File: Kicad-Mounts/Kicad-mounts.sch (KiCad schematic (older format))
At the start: 10 parts, among them P1 CONN_10, P2 CONN_10, P3 CONN_6X2, P6 CONN_3, U2 TPS77033

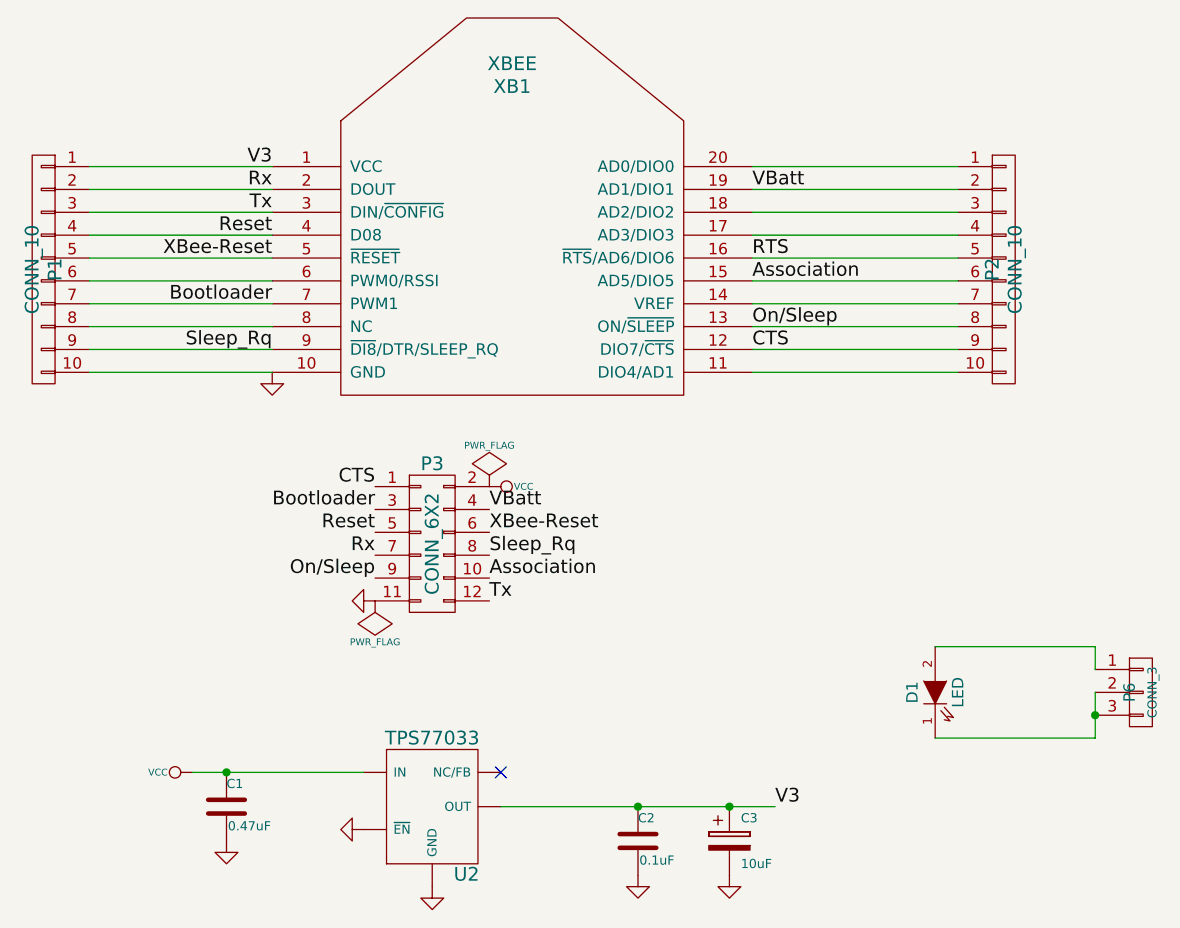
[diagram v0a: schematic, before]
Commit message: Major new version of the PCBs for next stage of production run.
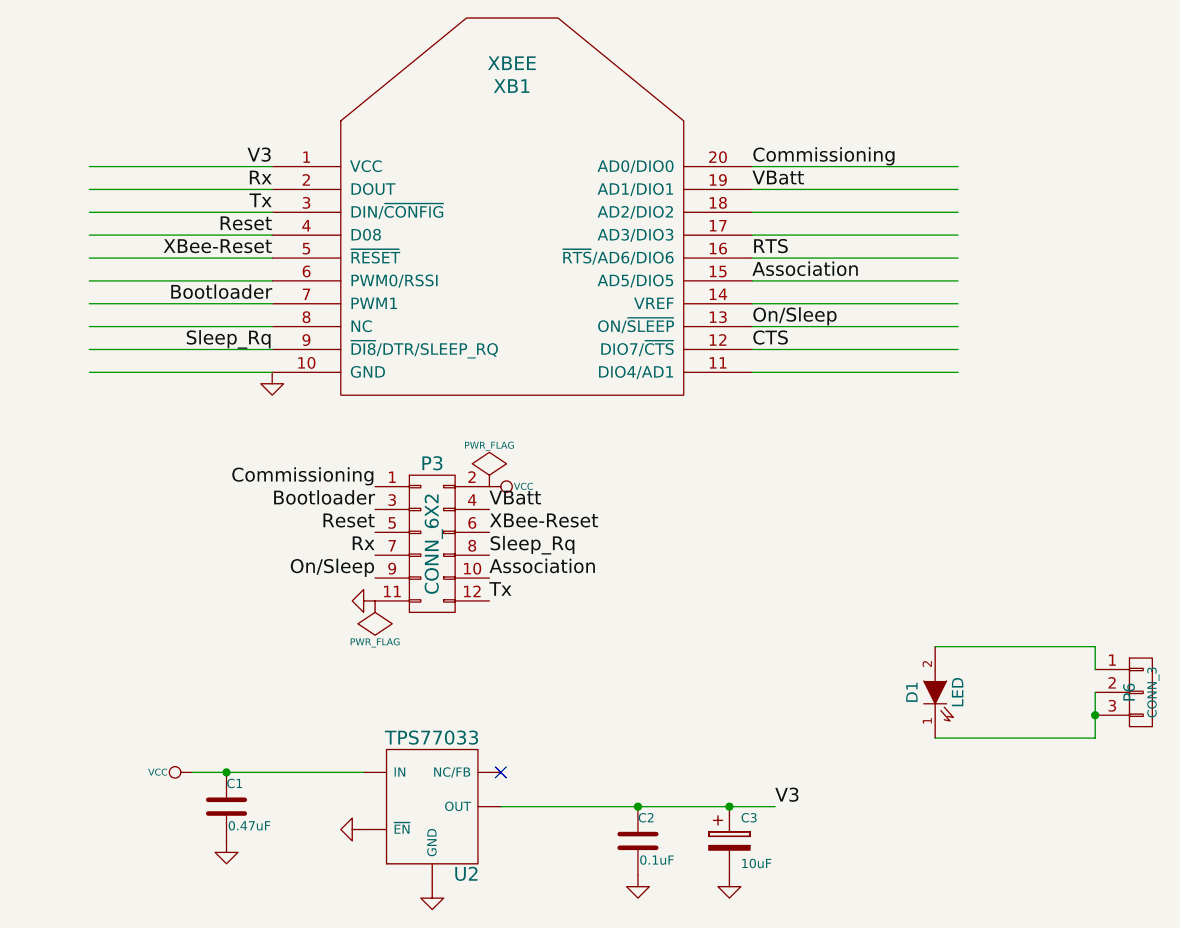
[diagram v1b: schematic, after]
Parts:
- removed P1, P2: CONN_10, Photodiode:SIL-10, symbol CONN_01X10
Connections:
- net labels added: Commissioning
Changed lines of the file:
@@
 encoding utf-8
 Sheet 1 1
-Title ""
-Date ""
-Rev ""
+Title "Watermeter XBee and LED Mounting Boards"
+Date "08 April 2016"
+Rev "1.00"
 Comp ""
 Comment1 ""
@@
 	1    4050 3850
 	1    0    0    -1
-$EndComp
-$Comp
-L CONN_02X06 P3
-U 1 1 53F67592
-P 3700 5050
-F 0 "P3" H 3700 5400 60  0000 C CNN
-F 1 "CONN_6X2" V 3700 5050 60  0000 C CNN
-F 2 "Photodiode:pin_header_2mm_2x6" H 3700 5050 60  0001 C CNN
-F 3 "" H 3700 5050 60  0000 C CNN
-	1    3700 5050
-	1    0    0    -1
-$EndComp
-$Comp
-L CONN_01X10 P2
-U 1 1 53F675C9
-P 6200 3850
-F 0 "P2" V 6150 3850 60  0000 C CNN
-F 1 "CONN_10" V 6250 3850 60  0000 C CNN
-F 2 "Photodiode:SIL-10" H 6200 3850 60  0001 C CNN
-F 3 "" H 6200 3850 60  0000 C CNN
-	1    6200 3850
-	1    0    0    -1
-$EndComp
-$Comp
-L CONN_01X10 P1
-U 1 1 53F6774F
-P 2000 3850
-F 0 "P1" V 1950 3850 60  0000 C CNN
-F 1 "CONN_10" V 2050 3850 60  0000 C CNN
-F 2 "Photodiode:SIL-10" H 2000 3850 60  0001 C CNN
-F 3 "" H 2000 3850 60  0000 C CNN
-	1    2000 3850
-	-1   0    0    -1
 $EndComp
 $Comp
@@
 	0    -1   -1   0
 $EndComp
-Wire Wire Line
-	6600 5600 6600 5500
-Wire Wire Line
-	6600 5500 5900 5500
-Wire Wire Line
-	6600 5700 6600 5900
-Wire Wire Line
-	6600 5900 5900 5900
-Wire Wire Line
-	2200 3400 3000 3400
-Wire Wire Line
-	2200 3500 3000 3500
-Wire Wire Line
-	2200 3600 3000 3600
-Wire Wire Line
-	2200 3700 3000 3700
-Wire Wire Line
-	2200 3800 3000 3800
-Wire Wire Line
-	2200 3900 3000 3900
-Wire Wire Line
-	2200 4000 3000 4000
-Wire Wire Line
-	2200 4100 3000 4100
-Wire Wire Line
-	2200 4200 3000 4200
-Wire Wire Line
-	2200 4300 3000 4300
-Wire Wire Line
-	5100 3400 6000 3400
-Wire Wire Line
-	5100 3500 6000 3500
-Wire Wire Line
-	5100 3600 6000 3600
-Wire Wire Line
-	5100 3700 6000 3700
-Wire Wire Line
-	5100 3800 6000 3800
-Wire Wire Line
-	5100 3900 6000 3900
-Wire Wire Line
-	5100 4000 6000 4000
-Wire Wire Line
-	5100 4100 6000 4100
-Wire Wire Line
-	5100 4200 6000 4200
-Wire Wire Line
-	5100 4300 6000 4300
 Text Label 3450 4900 2    60   ~ 0
 Bootloader
@@
 Rx
 Text Label 3450 4800 2    60   ~ 0
-CTS
+Commissioning
 Text Label 5100 3800 0    60   ~ 0
 RTS
@@
 Text Label 5100 3500 0    60   ~ 0
 VBatt
-Connection ~ 6600 5800
 $Comp
 L PWR_FLAG #FLG04
@@
 	1    0    0    -1
 $EndComp
-Wire Wire Line
-	2650 6050 3400 6050
-Wire Wire Line
-	4000 6200 5200 6200
-$Comp
-L GND #PWR07
+$Comp
+L GND #PWR06
 U 1 1 549A3CE1
 P 3700 6550
-F 0 "#PWR07" H 3700 6550 30  0001 C CNN
+F 0 "#PWR06" H 3700 6550 30  0001 C CNN
 F 1 "GND" H 3700 6480 30  0001 C CNN
 F 2 "" H 3700 6550 60  0000 C CNN
@@
 $EndComp
 $Comp
-L GND #PWR08
+L GND #PWR07
 U 1 1 549A3D0B
 P 4600 6500
-F 0 "#PWR08" H 4600 6500 30  0001 C CNN
+F 0 "#PWR07" H 4600 6500 30  0001 C CNN
 F 1 "GND" H 4600 6430 30  0001 C CNN
 F 2 "" H 4600 6500 60  0000 C CNN
@@
 $EndComp
 $Comp
-L GND #PWR09
+L GND #PWR08
 U 1 1 549A3D2E
 P 5000 6500
-F 0 "#PWR09" H 5000 6500 30  0001 C CNN
+F 0 "#PWR08" H 5000 6500 30  0001 C CNN
 F 1 "GND" H 5000 6430 30  0001 C CNN
 F 2 "" H 5000 6500 60  0000 C CNN
@@
 $EndComp
 $Comp
-L GND #PWR010
+L GND #PWR09
 U 1 1 549A3D51
 P 2800 6350
-F 0 "#PWR010" H 2800 6350 30  0001 C CNN
+F 0 "#PWR09" H 2800 6350 30  0001 C CNN
 F 1 "GND" H 2800 6280 30  0001 C CNN
 F 2 "" H 2800 6350 60  0000 C CNN
@@
 NoConn ~ 4000 6050
 $Comp
-L GND #PWR011
+L GND #PWR010
 U 1 1 549A3D98
 P 3400 6300
-F 0 "#PWR011" H 3400 6300 30  0001 C CNN
+F 0 "#PWR010" H 3400 6300 30  0001 C CNN
 F 1 "GND" H 3400 6230 30  0001 C CNN
 F 2 "" H 3400 6300 60  0000 C CNN
@@
 $EndComp
 $Comp
-L VCC #PWR012
+L VCC #PWR011
 U 1 1 549A5134
 P 2650 6050
-F 0 "#PWR012" H 2650 6150 30  0001 C CNN
+F 0 "#PWR011" H 2650 6150 30  0001 C CNN
 F 1 "VCC" V 2650 6200 30  0000 C CNN
 F 2 "" H 2650 6050 60  0000 C CNN
@@
 Text Label 5200 6200 0    60   ~ 0
 V3
+Text Label 5100 3900 0    60   ~ 0
+Association
+Wire Wire Line
+	6600 5600 6600 5500
+Wire Wire Line
+	6600 5500 5900 5500
+Wire Wire Line
+	6600 5700 6600 5900
+Wire Wire Line
+	6600 5900 5900 5900
+Wire Wire Line
+	2200 3400 3000 3400
+Wire Wire Line
+	2200 3500 3000 3500
+Wire Wire Line
+	2200 3600 3000 3600
+Wire Wire Line
+	2200 3700 3000 3700
+Wire Wire Line
+	2200 3800 3000 3800
+Wire Wire Line
+	2200 3900 3000 3900
+Wire Wire Line
+	2200 4000 3000 4000
+Wire Wire Line
+	2200 4100 3000 4100
+Wire Wire Line
+	2200 4200 3000 4200
+Wire Wire Line
+	2200 4300 3000 4300
+Wire Wire Line
+	5100 3400 6000 3400
+Wire Wire Line
+	5100 3500 6000 3500
+Wire Wire Line
+	5100 3600 6000 3600
+Wire Wire Line
+	5100 3700 6000 3700
+Wire Wire Line
+	5100 3800 6000 3800
+Wire Wire Line
+	5100 3900 6000 3900
+Wire Wire Line
+	5100 4000 6000 4000
+Wire Wire Line
+	5100 4100 6000 4100
+Wire Wire Line
+	5100 4200 6000 4200
+Wire Wire Line
+	5100 4300 6000 4300
+Connection ~ 6600 5800
+Wire Wire Line
+	2650 6050 3400 6050
+Wire Wire Line
+	4000 6200 5200 6200
 Connection ~ 5000 6200
 Connection ~ 4600 6200
 Connection ~ 2800 6050
-Text Label 5100 3900 0    60   ~ 0
-Association
+$Comp
+L CONN_02X06 P3
+U 1 1 53F67592
+P 3700 5050
+F 0 "P3" H 3700 5400 60  0000 C CNN
+F 1 "CONN_6X2" V 3700 5050 60  0000 C CNN
+F 2 "Photodiode:pin_header_2mm_2x6" H 3700 5050 60  0001 C CNN
+F 3 "" H 3700 5050 60  0000 C CNN
+	1    3700 5050
+	1    0    0    -1
+$EndComp
+Text Label 5100 3400 0    60   ~ 0
+Commissioning
 $EndSCHEMATC

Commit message: Update to a number of documents. Fix to Kicad-Mounts due to an obsoleted diode. Also a change to some command-line parameters for acqcontrol to line up with documented values.
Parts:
- D1: symbol LED -> LED-RESCUE-Kicad-mounts
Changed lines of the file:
@@
 EESchema Schematic File Version 2
+LIBS:Kicad-mounts-rescue
 LIBS:power
 LIBS:device
@@
 $EndComp
 $Comp
-L LED D1
+L LED-RESCUE-Kicad-mounts D1
 U 1 1 53F67A70
 P 5900 5700

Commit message: Minor change to Kicad-Mounts to remove dependence on rescue.lib
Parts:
- removed D1: LED, Photodiode:LED-mount, symbol LED-RESCUE-Kicad-mounts
- added D1: SFH4056, symbol LED_ALT
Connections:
- wire segments 26 -> 30
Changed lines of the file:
@@
 EESchema Schematic File Version 2
-LIBS:Kicad-mounts-rescue
 LIBS:power
 LIBS:device
@@
 	1    0    0    -1
 $EndComp
-$Comp
-L LED-RESCUE-Kicad-mounts D1
-U 1 1 53F67A70
-P 5900 5700
-F 0 "D1" H 5900 5800 50  0000 C CNN
-F 1 "LED" H 5900 5600 50  0000 C CNN
-F 2 "Photodiode:LED-mount" H 5900 5700 60  0001 C CNN
-F 3 "" H 5900 5700 60  0000 C CNN
-	1    5900 5700
-	0    -1   -1   0
-$EndComp
 Text Label 3450 4900 2    60   ~ 0
 Bootloader
@@
 	6600 5500 5900 5500
 Wire Wire Line
-	6600 5700 6600 5900
-Wire Wire Line
-	6600 5900 5900 5900
+	6600 5700 6600 5800
+Wire Wire Line
+	6600 5800 6600 5800
+Wire Wire Line
+	6600 5800 5900 5800
 Wire Wire Line
 	2200 3400 3000 3400
@@
 Connection ~ 6600 5800
 Wire Wire Line
-	2650 6050 3400 6050
-Wire Wire Line
-	4000 6200 5200 6200
+	2650 6050 2800 6050
+Wire Wire Line
+	2800 6050 3400 6050
+Wire Wire Line
+	4000 6200 4600 6200
+Wire Wire Line
+	4600 6200 5000 6200
+Wire Wire Line
+	5000 6200 5200 6200
 Connection ~ 5000 6200
 Connection ~ 4600 6200
@@
 Text Label 5100 3400 0    60   ~ 0
 Commissioning
+$Comp
+L LED_ALT D1
+U 1 1 5887D976
+P 5900 5650
+F 0 "D1" V 5900 5800 50  0000 C CNN
+F 1 "SFH4056" V 6150 5650 50  0000 C CNN
+F 2 "" H 5900 5650 50  0000 C CNN
+F 3 "" H 5900 5650 50  0000 C CNN
+	1    5900 5650
+	0    -1   -1   0
+$EndComp
 $EndSCHEMATC

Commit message: Update XBee symbol in node-test and mounts PCB schematics.
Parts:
- removed XB1: XBEE, Photodiode:XBee, symbol XBEE
- added XB?: XBEE-ZB, symbol XBEE-ZB
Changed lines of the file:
@@
 EESchema Schematic File Version 2
-LIBS:power
-LIBS:device
-LIBS:transistors
-LIBS:conn
-LIBS:linear
-LIBS:regul
-LIBS:74xx
-LIBS:cmos4000
-LIBS:adc-dac
-LIBS:memory
-LIBS:xilinx
-LIBS:microcontrollers
-LIBS:dsp
-LIBS:microchip
-LIBS:analog_switches
-LIBS:motorola
-LIBS:texas
-LIBS:intel
-LIBS:audio
-LIBS:interface
-LIBS:digital-audio
-LIBS:philips
-LIBS:display
-LIBS:cypress
-LIBS:siliconi
-LIBS:opto
-LIBS:atmel
-LIBS:contrib
-LIBS:valves
+LIBS:DataStorage
 LIBS:KB1LQC
 LIBS:MiscellaneousDevices
+LIBS:RF_OEM_Parts
 LIBS:Sensors
-LIBS:RF_OEM_Parts
 LIBS:Kicad-mounts-cache
 EELAYER 25 0
@@
 Comment4 ""
 $EndDescr
-$Comp
-L XBEE XB1
-U 1 1 53F67332
-P 4050 3850
-F 0 "XB1" H 4050 4650 60  0000 C CNN
-F 1 "XBEE" H 4050 4750 60  0000 C CNN
-F 2 "Photodiode:XBee" H 4050 3850 60  0001 C CNN
-F 3 "" H 4050 3850 60  0000 C CNN
-	1    4050 3850
-	1    0    0    -1
-$EndComp
 $Comp
 L CONN_01X03 P6
@@
 	0    -1   -1   0
 $EndComp
+$Comp
+L XBEE-ZB XB?
+U 1 1 58B79FBE
+P 4050 3850
+F 0 "XB?" H 4050 4650 60  0000 C CNN
+F 1 "XBEE-ZB" H 4050 4750 60  0000 C CNN
+F 2 "" H 4050 3850 60  0000 C CNN
+F 3 "" H 4050 3850 60  0000 C CNN
+	1    4050 3850
+	1    0    0    -1
+$EndComp
 $EndSCHEMATC
